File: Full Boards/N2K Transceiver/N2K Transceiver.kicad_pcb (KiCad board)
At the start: 4 copper layers, 80 x 60 mm, 75 parts, among them J3 JTAG, SW1 SW_MEC_5G, SW2 SW_MEC_5G, SW3 SW_MEC_5G

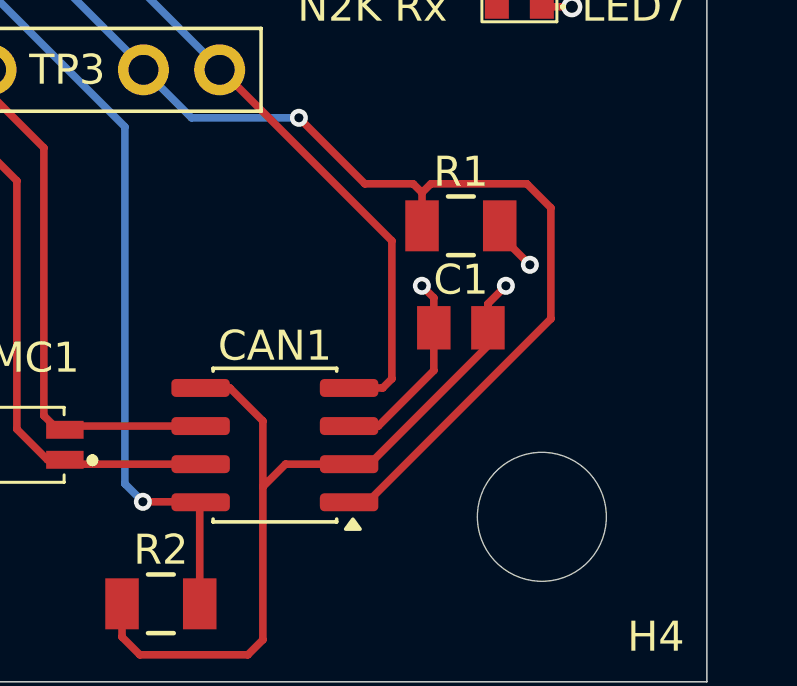
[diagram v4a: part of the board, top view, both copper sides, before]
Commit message: Slightly closed the distance between CAN1 and C1.
Signed-off-by: digimer <digital.mermaid@gmail.com>
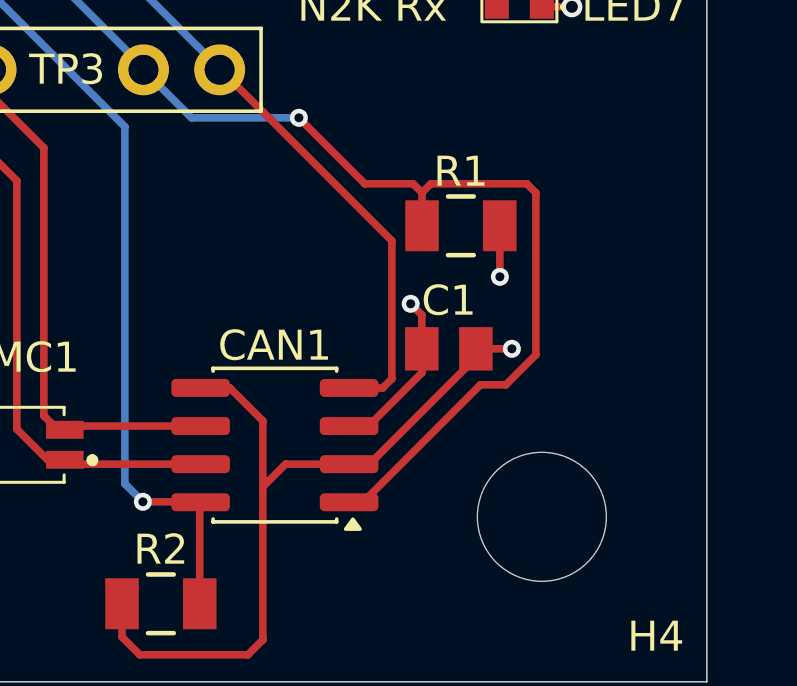
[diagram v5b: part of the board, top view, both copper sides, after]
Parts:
- moved C1 0.81 mm to (131.4, 92.2)
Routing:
- net +3.3V: track 79.5 -> 78.5 mm
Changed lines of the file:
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@@
 	(footprint "mr-stuff:Kyocera AVX 0805"
 		(layer "F.Cu")
-		(at 131.8 91.5 180)
+		(at 131.4 92.2 180)
 		(tags "08051C105K4Z2A ")
 		(property "Reference" "C1"
@@
 			(polygon
 				(pts
-					(xy 132.0921 92.1731) (xy 131.5079 92.1731) (xy 131.5079 90.8269) (xy 132.0921 90.8269)
+					(xy 131.6921 92.8731) (xy 131.1079 92.8731) (xy 131.1079 91.5269) (xy 131.6921 91.5269)
 				)
 			)
@@
 	)
 	(segment
-		(start 133.0954 88.3954)
-		(end 134.1 89.4)
+		(start 103.403416 77.645916)
+		(end 103.0575 77.3)
 		(width 0.254)
 		(layer "F.Cu")
@@
 	)
 	(segment
-		(start 103.403416 77.645916)
-		(end 103.0575 77.3)
+		(start 83.01 80.76)
+		(end 82.5 80.25)
 		(width 0.254)
 		(layer "F.Cu")
@@
 	)
 	(segment
-		(start 83.01 80.76)
-		(end 82.5 80.25)
+		(start 133.0954 88.3954)
+		(end 133.1 88.4)
 		(width 0.254)
 		(layer "F.Cu")
@@
 	)
 	(segment
-		(start 130.8983 91.5)
-		(end 130.8983 90.4983)
+		(start 130.4983 91.0713)
+		(end 130.4983 92.2)
 		(width 0.254)
 		(layer "F.Cu")
@@
 	)
 	(segment
+		(start 128.725 94.775)
+		(end 130.4983 93.0017)
+		(width 0.254)
+		(layer "F.Cu")
+		(net "+3.3V")
+	)
+	(segment
 		(start 103.2608 76.375916)
 		(end 103.047108 76.589608)
@@
 	)
 	(segment
+		(start 130.127 90.7)
+		(end 130.4983 91.0713)
+		(width 0.254)
+		(layer "F.Cu")
+		(net "+3.3V")
+	)
+	(segment
 		(start 91.25 46.01)
 		(end 88.2637 46.01)
@@
 	)
 	(segment
-		(start 129.049999 94.775)
-		(end 130.8983 92.926699)
+		(start 103.0575 77.3)
+		(end 103.0575 76.6)
 		(width 0.254)
 		(layer "F.Cu")
@@
 	)
 	(segment
-		(start 103.0575 77.3)
-		(end 103.0575 76.6)
+		(start 114.2983 76.4983)
+		(end 112.9 76.4983)
 		(width 0.254)
 		(layer "F.Cu")
@@
 	)
 	(segment
-		(start 130.8983 92.926699)
-		(end 130.8983 91.5)
+		(start 128.075 94.775)
+		(end 128.725 94.775)
 		(width 0.254)
 		(layer "F.Cu")
@@
 	)
 	(segment
-		(start 114.2983 76.4983)
-		(end 112.9 76.4983)
+		(start 81 81.25)
+		(end 81 82.6)
 		(width 0.254)
 		(layer "F.Cu")
@@
 	)
 	(segment
-		(start 81 81.25)
-		(end 81 82.6)
+		(start 130.4983 93.0017)
+		(end 130.4983 92.2)
 		(width 0.254)
 		(layer "F.Cu")
@@
 	)
 	(segment
-		(start 128.075 94.775)
-		(end 129.049999 94.775)
+		(start 81.5 82.4)
+		(end 84.247 85.147)
 		(width 0.254)
 		(layer "F.Cu")
@@
 	)
 	(segment
-		(start 81.5 82.4)
-		(end 84.247 85.147)
+		(start 133.1 88.4)
+		(end 133.1 89.8)
 		(width 0.254)
 		(layer "F.Cu")
@@
 	)
 	(segment
-		(start 130.8983 90.4983)
-		(end 130.5 90.1)
-		(width 0.254)
-		(layer "F.Cu")
-		(net "+3.3V")
-	)
-	(segment
 		(start 109.8325 69.575916)
 		(end 104.8825 69.575916)
@@
 	)
 	(via
-		(at 130.5 90.1)
+		(at 130.127 90.7)
 		(size 0.6)
 		(drill 0.3)
@@
 	)
 	(via
-		(at 134.1 89.4)
+		(at 133.1 89.8)
 		(size 0.6)
 		(drill 0.3)
@@
 	)
 	(segment
-		(start 132.7017 91.5)
-		(end 132.7017 90.6983)
-		(width 0.254)
-		(layer "F.Cu")
-		(net "GND")
-	)
-	(segment
 		(start 121.0997 102.4)
 		(end 124.7 102.4)
@@
 	)
 	(segment
-		(start 132.7017 90.6983)
-		(end 133.3 90.1)
-		(width 0.254)
-		(layer "F.Cu")
-		(net "GND")
-	)
-	(segment
 		(start 134.5 63.4)
 		(end 135.5 63.4)
@@
 	)
 	(segment
-		(start 132.7017 92.0983)
-		(end 128.755 96.045)
+		(start 108.75 44.74)
+		(end 109.96 44.74)
 		(width 0.254)
 		(layer "F.Cu")
@@
 	)
 	(segment
-		(start 108.75 44.74)
-		(end 109.96 44.74)
+		(start 133.5 92.2)
+		(end 132.3017 92.2)
 		(width 0.254)
 		(layer "F.Cu")
@@
 	)
 	(segment
+		(start 128.755 96.045)
+		(end 132.3017 92.4983)
+		(width 0.254)
+		(layer "F.Cu")
+		(net "GND")
+	)
+	(segment
 		(start 106.3575 71.599116)
 		(end 106.3575 72.895916)
@@
 	)
 	(segment
+		(start 132.3017 92.4983)
+		(end 132.3017 92.2)
+		(width 0.254)
+		(layer "F.Cu")
+		(net "GND")
+	)
+	(segment
 		(start 63.6046 75.6)
 		(end 63.6046 74.5046)
@@
 	)
 	(segment
+		(start 128.075 96.045)
+		(end 128.755 96.045)
+		(width 0.254)
+		(layer "F.Cu")
+		(net "GND")
+	)
+	(segment
 		(start 134.5 69.2)
 		(end 135.5 69.2)
@@
 	)
 	(via
-		(at 133.3 90.1)
+		(at 133.5 92.2)
 		(size 0.6)
 		(drill 0.3)
@@
 	)
 	(segment
+		(start 134.3 92.4)
+		(end 133.3 93.4)
+		(width 0.254)
+		(layer "F.Cu")
+		(net "/CAN_TX_LOCAL")
+	)
+	(segment
 		(start 130.2095 86.7)
 		(end 130.5046 86.9951)
@@
 	)
 	(segment
-		(start 130.5046 86.9951)
-		(end 130.7997 86.7)
+		(start 132.45 93.4)
+		(end 128.685 97.165)
+		(width 0.254)
+		(layer "F.Cu")
+		(net "/CAN_TX_LOCAL")
+	)
+	(segment
+		(start 133.3 93.4)
+		(end 132.45 93.4)
+		(width 0.254)
+		(layer "F.Cu")
+		(net "/CAN_TX_LOCAL")
+	)
+	(segment
+		(start 130.7997 86.7)
+		(end 134 86.7)
 		(width 0.254)
 		(layer "F.Cu")
@@
 	)
 	(segment
-		(start 134.8 87.5)
-		(end 134.8 91.2)
+		(start 128.685 97.165)
+		(end 128.685 97.315)
 		(width 0.254)
 		(layer "F.Cu")
@@
 	)
 	(segment
-		(start 105.5385 64.077)
-		(end 105.5385 64.0615)
+		(start 134.3 87)
+		(end 134.3 92.4)
 		(width 0.254)
 		(layer "F.Cu")
@@
 	)
 	(segment
-		(start 126.4 84.5)
-		(end 128.6 86.7)
+		(start 105.5385 64.077)
+		(end 105.5385 64.0615)
 		(width 0.254)
 		(layer "F.Cu")
@@
 	)
 	(segment
-		(start 130.7997 86.7)
-		(end 134 86.7)
+		(start 126.4 84.5)
+		(end 128.6 86.7)
 		(width 0.254)
 		(layer "F.Cu")
@@
 	(segment
 		(start 134 86.7)
-		(end 134.8 87.5)
+		(end 134.3 87)
 		(width 0.254)
 		(layer "F.Cu")
@@
 	)
 	(segment
-		(start 134.8 91.2)
-		(end 128.685 97.315)
+		(start 130.5046 86.9951)
+		(end 130.7997 86.7)
 		(width 0.254)
 		(layer "F.Cu")

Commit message: Swapped 1A VR for 600mA version.
Signed-off-by: digimer <digital.mermaid@gmail.com>
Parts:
- VR1: value TPSM33610S3QRDNRQ1 -> TPSM33606S3QRDNRQ1
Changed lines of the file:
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@@
 			)
 		)
-		(property "Value" "TPSM33610S3QRDNRQ1"
+		(property "Value" "TPSM33606S3QRDNRQ1"
 			(at 0 5.5 0)
 			(unlocked yes)

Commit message: Cleaned up silkscreen.
Signed-off-by: digimer <digital.mermaid@gmail.com>
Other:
- board text added: "-=] J1 - JTAG 1. GND 2. MTS (MTMS - IO42) 3. TDI (MTDI - IO41) 4. TDO (MTDO - IO40) 5. TCK (MTCK - IO39)"
- board text added: "-=] TP1 - MCU 1. +3.3V 2. TXDO 3. RXDO 4. GND"
- board text added: "-=] TP2 - CAN 1. CAN-High 2. CAN-Low 3. n/c 4. CAN-Tx (Local) 5. CAN-Rx (Local)"
- board text added: "Pinouts on reverse side"
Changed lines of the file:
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@@
 	(title_block
 		(title "N2K Transceiver")
-		(date "2026-09-02")
+		(date "2026-09-11")
 		(rev "1.0.0")
 		(company "Mermaid's Rest")
@@
 		(tags "mountinghole M4")
 		(property "Reference" "H4"
-			(at 3.8 4 0)
+			(at 3.9 4.2 0)
 			(layer "F.SilkS")
 			(effects
@@
 		(tags "08051C105K4Z2A ")
 		(property "Reference" "C13"
-			(at 3.2017 0 0)
+			(at 0 -1.7 0)
 			(unlocked yes)
 			(layer "F.SilkS")
@@
 		(tags "mountinghole M4")
 		(property "Reference" "H3"
-			(at 3.8 -4.2 0)
+			(at 3.9 -4.2 0)
 			(layer "F.SilkS")
 			(effects
@@
 		(tags "mountinghole M4")
 		(property "Reference" "H1"
-			(at -4.1 -4.1 0)
+			(at -3.9 -4.2 0)
 			(layer "F.SilkS")
 			(effects
@@
 		)
 	)
+	(gr_circle
+		(center 65.5 48.8)
+		(end 69.9 48.8)
+		(stroke
+			(width 0.15)
+			(type solid)
+		)
+		(fill no)
+		(layer "F.SilkS")
+	)
+	(gr_circle
+		(center 65.5 97.8)
+		(end 69.9 97.8)
+		(stroke
+			(width 0.15)
+			(type solid)
+		)
+		(fill no)
+		(layer "F.SilkS")
+	)
+	(gr_circle
+		(center 134.5 48.8)
+		(end 138.9 48.8)
+		(stroke
+			(width 0.15)
+			(type solid)
+		)
+		(fill no)
+		(layer "F.SilkS")
+	)
+	(gr_circle
+		(center 134.5 97.8)
+		(end 138.9 97.8)
+		(stroke
+			(width 0.15)
+			(type solid)
+		)
+		(fill no)
+		(layer "F.SilkS")
+	)
 	(gr_rect
 		(start 60 43.3)
@@
 	)
 	(gr_text "N2K Transceiver\n© Tuskar Marine\nv1.0.0 - 2026"
-		(at 69 50.9 0)
+		(at 70.3 48.9 0)
 		(layer "F.SilkS")
 		(effects
@@
 		)
 	)
+	(gr_text "Pinouts on\nreverse side"
+		(at 115.3 56.7 0)
+		(layer "F.SilkS")
+		(effects
+			(font
+				(size 1 1)
+				(thickness 0.15)
+			)
+			(justify left)
+		)
+	)
 	(gr_text "Server Link"
 		(at 127.45 69.2 0)
@@
 		)
 	)
+	(gr_text "-=] TP1 - MCU\n1. +3.3V\n2. TXDO\n3. RXDO\n4. GND"
+		(at 114.8 44.1 0)
+		(layer "B.SilkS")
+		(effects
+			(font
+				(size 1 1)
+				(thickness 0.15)
+			)
+			(justify left top mirror)
+		)
+	)
+	(gr_text "-=] TP2 - CAN\n1. CAN-High\n2. CAN-Low\n3. n/c\n4. CAN-Tx (Local)\n5. CAN-Rx (Local)"
+		(at 125 71.7 0)
+		(layer "B.SilkS")
+		(effects
+			(font
+				(size 1 1)
+				(thickness 0.15)
+			)
+			(justify left top mirror)
+		)
+	)
+	(gr_text "-=] J1 - JTAG\n1. GND\n2. MTS (MTMS - IO42)\n3. TDI (MTDI - IO41)\n4. TDO (MTDO - IO40)\n5. TCK (MTCK - IO39)"
+		(at 129.36 51.08 0)
+		(layer "B.SilkS")
+		(effects
+			(font
+				(size 1 1)
+				(thickness 0.15)
+			)
+			(justify left top mirror)
+		)
+	)
